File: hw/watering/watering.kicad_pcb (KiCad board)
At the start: 2 copper layers, 262 x 50 mm, 103 parts, among them J2 USB_C_Receptacle, J3 Conn_01x02_Pin, J4 Conn_01x02_Pin, J6 Conn_01x02_Pin, Q1 2N7002, SW2 KMS221GLFS, SW3 KMS221GLFS, U1 ESP32-C6, U10 MCP6002-xSN, U11 STI3508, U2 DRV8220DSG, U3 W25Q128JVS, U4 STI3508, U5 STI3508, U6 STI3508, U7 NCP163AFCT330T2G, U8 MCP6002-xSN, U9 MCP6002-xSN, Y1 40MHz, Y2 32768Hz

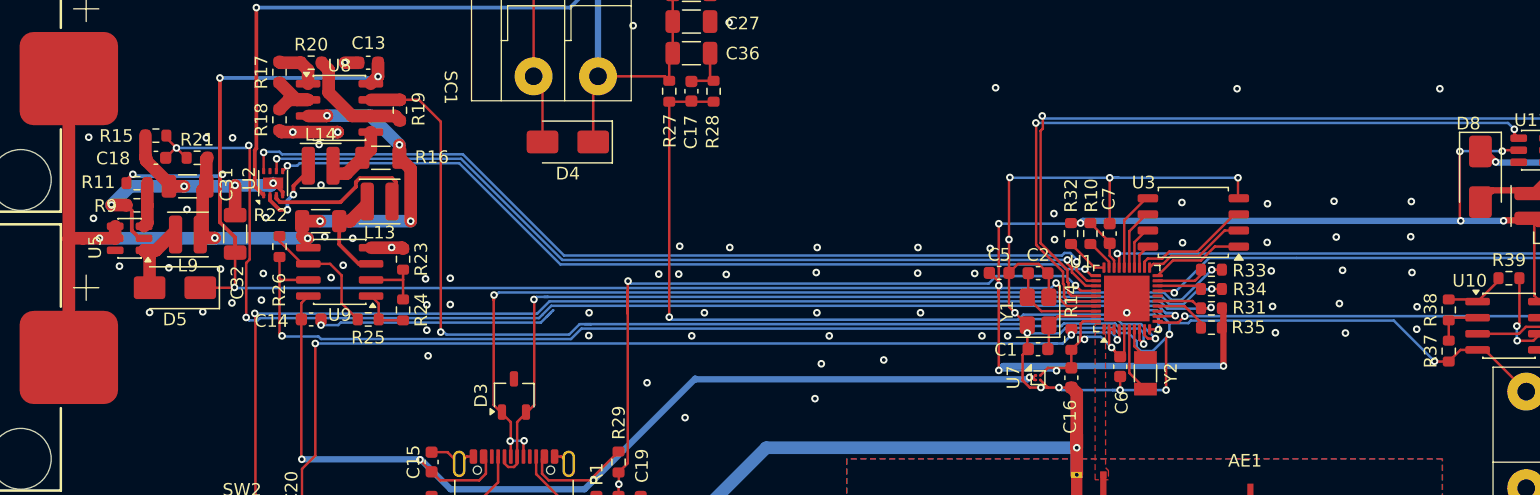
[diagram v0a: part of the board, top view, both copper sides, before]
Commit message: - improved voltage boost on battery power - some issues with rtc clock - some issues with pwm that result in brownout
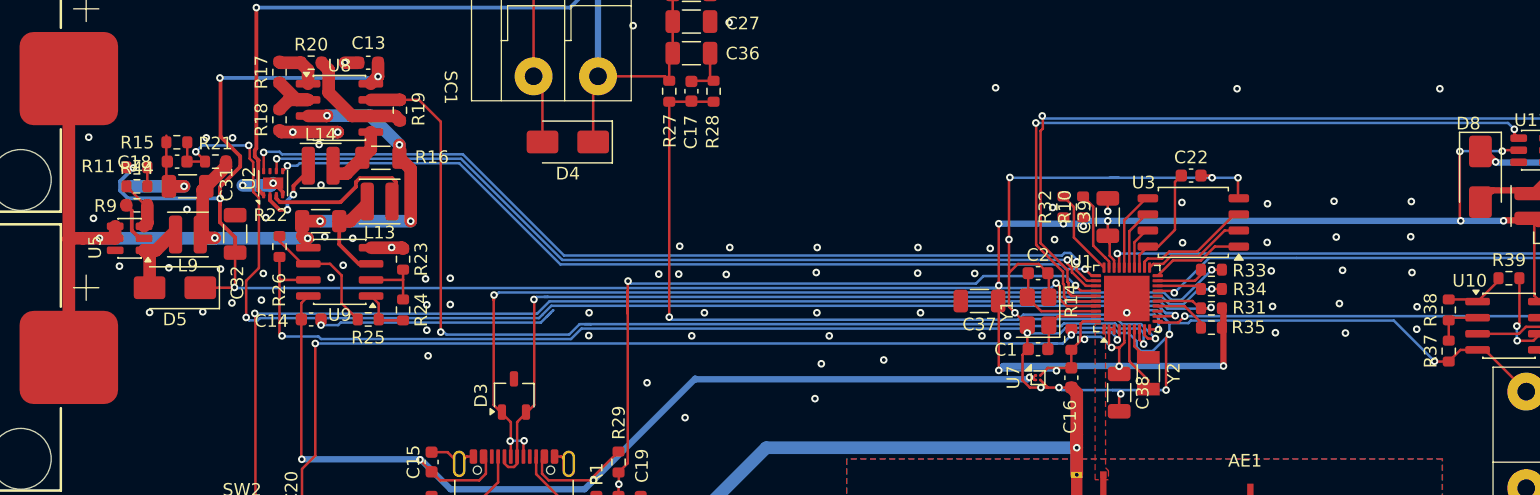
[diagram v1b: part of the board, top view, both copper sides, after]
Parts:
- removed C5, C6, C7: 100n, Capacitor_SMD:C_0603_1608Metric
- added C22: 1u, Capacitor_SMD:C_0603_1608Metric, F.Cu at (193.2, 120.7)
- added C37: 22u, Capacitor_SMD:C_1206_3216Metric, F.Cu at (176.5, 130.6)
- added C38: 22u, Capacitor_SMD:C_1206_3216Metric, F.Cu at (187.5, 137.8)
- added C39: 22u, Capacitor_SMD:C_1206_3216Metric, F.Cu at (186.6, 123.9)
- added R44: 15k, Resistor_SMD:R_0603_1608Metric, F.Cu at (110.0, 121.5)
- R11: value 47k -> 30k
- moved R32 2.18 mm to (183.1, 123.1), turned to 90 degrees
- moved R10 2.18 mm to (184.7, 123.1), turned to 90 degrees
- moved R15 1.73 mm to (113.2, 118.0)
- moved C18 1.70 mm to (113.2, 119.5)
- moved R21 1.48 mm to (116.2, 119.5)
- moved R11 1.25 mm to (110.0, 120.0)
- moved Y2 0.23 mm to (189.8, 136.2)
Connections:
- R11 pad 1: /solar/0V6 -> Net-(R11-Pad1)
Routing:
- net /GND: track 329.4 -> 317.0 mm
- net Net-(U1-VDD_SPI/GPIO27): track 1.93 -> 9.11 mm
- net /controller/SDA: track 2.51 -> 6.46 mm
- net /controller/SCL: track 3.37 -> 6.94 mm
- net /+3V3: track 299.3 -> 301.7 mm, vias 24 -> 27
- net Net-(R11-Pad1): track 0.00 -> 1.50 mm
- net /solar/0V6: track 3.51 -> 4.03 mm

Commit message: - fixed formatting - proper pwm output for conductivity output
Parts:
- removed R29: 47k, Resistor_SMD:R_0603_1608Metric
- added R45: 10k, Resistor_SMD:R_0603_1608Metric, F.Cu at (148.0, 143.2)
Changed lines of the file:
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@@
 		)
 	)
+	(footprint "Resistor_SMD:R_0603_1608Metric"
+		(layer "F.Cu")
+		(at 148 143.25 -90)
+		(descr "Resistor SMD 0603 (1608 Metric), square (rectangular) end terminal, IPC-7351 nominal, (Body size source: IPC-SM-782 page 72, https://www.pcb-3d.com/wordpress/wp-content/uploads/ipc-sm-782a_amendment_1_and_2.pdf)")
+		(tags "resistor")
+		(property "Reference" "R45"
+			(at -2.85 -0.025 90)
+			(layer "F.SilkS")
+			(effects
+				(font
+					(size 1 1)
+					(thickness 0.15)
+				)
+			)
+		)
+		(property "Value" "10k"
+			(at -0.075 -0.025 90)
+			(layer "F.Fab")
+			(effects
+				(font
+					(size 1 1)
+					(thickness 0.15)
+				)
+			)
+		)
+		(property "Datasheet" "https://jlc-prod-smt.oss-eu-central-1.aliyuncs.com/smtDataManualFile/8579706381316128768-C25804.pdf?response-content-disposition=attachment%3B%20filename%3DC25804.pdf%3B%20filename%2A%3DUTF-8%27%27C25804.pdf&x-oss-date=20260604T182440Z&x-oss-expires=1800&x-oss-security-token=CAISgAN1q6Ft5B2yfSjIr5nhDvTiu55L8aayRHLFsEERZtthpKj%2B0Dz2IHhMdHJsAOodtv0%2FmmhT6PkclqRLcbhpcmfjV%2BZHzLB8qeRniENA4J7b16cNrbH4M4H6aXeirtuwDsz9SNTCALjPD3nPii50x5bjaDymRCbLGJaViJlhHLN1Ow6jdmhpCctxLAlvo9NgFxm3D%2Fu2NQPwiWf9FVdhvhEG6Vly8qOi2MaRmFy8yFTx0b0SvJ%2BjYMrmPctoN9JnSdC5mfdzau3a1TJ84gRD0a5wkaVA1zbDs5bfISEIuUzebreLqY03dV4mOvdqIcMe8qigz88fk%2FfIioH6xyxKOexoSCnFTOiiupCcQLPyao9jLu6iayqViY7QaIOTqQohZmkAMwVOasAsI3Ngh4zF97Qt0cVNkXO9gWfLI8DtuMleWhri1Udu3tHD0eS19jklBdzSlusJRAJJUVBflCeKEaRNSAd3WGhEfM2%2BBt4QT30w5N2u00S8OSMIOONBvqKWD5sagAGpldF62iBeHzrNV%2BHnUyjaA64BCjacRbVbSjmxSgiuNX1d%2FbCnqQV25prdqNhtDbAKCoRnNQDFNxmhLIIUUcffM9eG3oRc44RNhyi7hADN6z1ILjt6TEoRuXkDAYH1u8iyrE2YQDMkq7F3Cke8dxQ44PYZqWefci6GHDzQ1pzPpiAA&x-oss-signature-version=OSS4-HMAC-SHA256&x-oss-credential=STS.NZTENVVAjFdYFTtTADjTMKmU2%2F20260604%2Feu-central-1%2Foss%2Faliyun_v4_request&x-oss-signature=78c2b620008555fdaf271c3d0b7682edd0aca7d23428d31f63338848e1713cab"
+			(at 0 0 90)
+			(layer "F.Fab")
+			(hide yes)
+			(effects
+				(font
+					(size 1.27 1.27)
+				)
+			)
+		)
+		(property "Description" "C25804"
+			(at 0 0 90)
+			(layer "F.Fab")
+			(hide yes)
+			(effects
+				(font
+					(size 1.27 1.27)
+				)
+			)
+		)
+		(property "KiLib_Generator" "SMD_2terminal_chip_molded"
+			(at 0 0 90)
+			(layer "F.SilkS")
+			(hide yes)
+			(effects
+				(font
+					(size 1 1)
+					(thickness 0.15)
+				)
+			)
+		)
+		(property ki_fp_filters "R_*")
+		(sheetname "/")
+		(sheetfile "watering.kicad_sch")
+		(units
+			(unit
+				(name "A")
+				(pins "1" "2")
+			)
+		)
+		(attr smd)
+		(duplicate_pad_numbers_are_jumpers no)
+		(fp_line
+			(start -0.237258 0.5225)
+			(end 0.237258 0.5225)
+			(stroke
+				(width 0.12)
+				(type solid)
+			)
+			(layer "F.SilkS")
+		)
+		(fp_line
+			(start -0.237258 -0.5225)
+			(end 0.237258 -0.5225)
+			(stroke
+				(width 0.12)
+				(type solid)
+			)
+			(layer "F.SilkS")
+		)
+		(fp_rect
+			(start -1.48 -0.73)
+			(end 1.48 0.73)
+			(stroke
+				(width 0.05)
+				(type solid)
+			)
+			(fill no)
+			(layer "F.CrtYd")
+		)
+		(fp_rect
+			(start -0.8 -0.4125)
+			(end 0.8 0.4125)
+			(stroke
+				(width 0.1)
+				(type solid)
+			)
+			(fill no)
+			(layer "F.Fab")
+		)
+		(fp_text user "${REFERENCE}"
+			(at 0 0 90)
+			(layer "F.Fab")
+			(effects
+				(font
+					(size 0.4 0.4)
+					(thickness 0.06)
+				)
+			)
+		)
+		(pad "1" smd roundrect
+			(at -0.825 0 270)
+			(size 0.8 0.95)
+			(layers "F.Cu" "F.Mask" "F.Paste")
+			(roundrect_rratio 0.25)
+			(net "/+5V")
+			(pintype "passive")
+		)
+		(pad "2" smd roundrect
+			(at 0.825 0 270)
+			(size 0.8 0.95)
+			(layers "F.Cu" "F.Mask" "F.Paste")
+			(roundrect_rratio 0.25)
+			(net "/V_usb_avail")
+			(pintype "passive")
+		)
+		(embedded_fonts no)
+		(model "${KICAD10_3DMODEL_DIR}/Resistor_SMD.3dshapes/R_0603_1608Metric.step"
+			(offset
+				(xyz 0 0 0)
+			)
+			(scale
+				(xyz 1 1 1)
+			)
+			(rotate
+				(xyz 0 0 0)
+			)
+		)
+	)
 	(footprint "Capacitor_SMD:C_1206_3216Metric"
 		(layer "F.Cu")
@@
 		(tags "capacitor")
 		(property "Reference" "C38"
-			(at 0 -1.85 90)
+			(at 3.825 -0.175 90)
 			(layer "F.SilkS")
 			(effects
@@
 		)
 		(property "Value" "22u"
-			(at 0 1.85 90)
+			(at 0.05 0 90)
 			(layer "F.Fab")
 			(effects
@@
 			(layer "F.Fab")
 		)
-		(fp_text user "${REFERENCE}"
-			(at 0 0 90)
-			(layer "F.Fab")
-			(effects
-				(font
-					(size 0.8 0.8)
-					(thickness 0.12)
-				)
-			)
-		)
 		(pad "1" smd roundrect
 			(at -1.475 0 270)
@@
 		)
 	)
-	(footprint "Resistor_SMD:R_0603_1608Metric"
-		(layer "F.Cu")
-		(at 148 143.25 90)
-		(descr "Resistor SMD 0603 (1608 Metric), square (rectangular) end terminal, IPC-7351 nominal, (Body size source: IPC-SM-782 page 72, https://www.pcb-3d.com/wordpress/wp-content/uploads/ipc-sm-782a_amendment_1_and_2.pdf)")
-		(tags "resistor")
-		(property "Reference" "R29"
-			(at 3.1 0.025 90)
-			(layer "F.SilkS")
-			(effects
-				(font
-					(size 1 1)
-					(thickness 0.15)
-				)
-			)
-		)
-		(property "Value" "47k"
-			(at -0.025 0.125 90)
-			(layer "F.Fab")
-			(effects
-				(font
-					(size 1 1)
-					(thickness 0.15)
-				)
-			)
-		)
-		(property "Datasheet" "https://jlc-prod-smt.oss-eu-central-1.aliyuncs.com/smtDataManualFile/8579706364622934016-C25819.pdf?response-content-disposition=attachment%3B%20filename%3DC25819.pdf%3B%20filename%2A%3DUTF-8%27%27C25819.pdf&x-oss-date=20260607T210642Z&x-oss-expires=1800&x-oss-security-token=CAISgAN1q6Ft5B2yfSjIr5ryH8PCprRbhIysal7ylzcBXuxKqZznuzz2IHhMdHJsAOodtv0%2FmmhT6PkclqRLcbhpcmfjV%2BZHzLB8qbxek0BD4J7b16cNrbH4M4H6aXeirtuwDsz9SNTCALjPD3nPii50x5bjaDymRCbLGJaViJlhHLN1Ow6jdmhpCctxLAlvo9NgFxm3D%2Fu2NQPwiWf9FVdhvhEG6Vly8qOi2MaRmFy8yFTx0b0SvJ%2BjYMrmPctoN9JnSdC5mfdzau3a1TJ84gRD0a5wkaVA1zbDs5bfISEIuUzebreLqY03dV4mOvdqIcMe8qigz88fk%2FfIioH6xyxKOexoSCnFTOiiupCcQLPyao9jLu6iayqViY7QaIOTqQohZmkAMwVOasAsI3Ngh4zF97Qt0cVNkXO9gWfLI8DtuMleWkpjUPw8wnSgc5lCkRRYwGs1287ugXlSQzo890KPDAEovaKCnZ2ZSfh7Y4sNknI6i%2Bfc2Se2MIkIuzN54aKWD5sagAFXqr37yeC6i73JtnWyrAPWlFlD7%2BO4v6D0kklJkfR4ZNWYY%2FJmHaMvh5XgKe69Y2VVwh3FQXeQc9N3YnYUCwlUFj7ysfoRU0zIPvuKAhEOT3qEObty6yli3txhJK%2BkEcQ4NQs%2FlNRRqPdiq%2BB4j8AoteNyHTVnRr3qFmKb96GmHCAA&x-oss-signature-version=OSS4-HMAC-SHA256&x-oss-credential=STS.NYGTyvKkz3NGhxCs7TRcfFYLY%2F20260607%2Feu-central-1%2Foss%2Faliyun_v4_request&x-oss-signature=d302d6996d62a00132e559a883be9b5fca7841b1eb7e44c91ba09bae985432b1"
-			(at 0 0 90)
-			(layer "F.Fab")
-			(hide yes)
-			(effects
-				(font
-					(size 1.27 1.27)
-				)
-			)
-		)
-		(property "Description" "C25819"
-			(at 0 0 90)
-			(layer "F.Fab")
-			(hide yes)
-			(effects
-				(font
-					(size 1.27 1.27)
-				)
-			)
-		)
-		(property "KiLib_Generator" "SMD_2terminal_chip_molded"
-			(at 0 0 90)
-			(layer "F.SilkS")
-			(hide yes)
-			(effects
-				(font
-					(size 1 1)
-					(thickness 0.15)
-				)
-			)
-		)
-		(property ki_fp_filters "R_*")
-		(sheetname "/")
-		(sheetfile "watering.kicad_sch")
-		(units
-			(unit
-				(name "A")
-				(pins "1" "2")
-			)
-		)
-		(attr smd)
-		(duplicate_pad_numbers_are_jumpers no)
-		(fp_line
-			(start -0.237258 -0.5225)
-			(end 0.237258 -0.5225)
-			(stroke
-				(width 0.12)
-				(type solid)
-			)
-			(layer "F.SilkS")
-		)
-		(fp_line
-			(start -0.237258 0.5225)
-			(end 0.237258 0.5225)
-			(stroke
-				(width 0.12)
-				(type solid)
-			)
-			(layer "F.SilkS")
-		)
-		(fp_rect
-			(start -1.48 -0.73)
-			(end 1.48 0.73)
-			(stroke
-				(width 0.05)
-				(type solid)
-			)
-			(fill no)
-			(layer "F.CrtYd")
-		)
-		(fp_rect
-			(start -0.8 -0.4125)
-			(end 0.8 0.4125)
-			(stroke
-				(width 0.1)
-				(type solid)
-			)
-			(fill no)
-			(layer "F.Fab")
-		)
-		(pad "1" smd roundrect
-			(at -0.825 0 90)
-			(size 0.8 0.95)
-			(layers "F.Cu" "F.Mask" "F.Paste")
-			(roundrect_rratio 0.25)
-			(net "/V_usb_avail")
-			(pintype "passive")
-		)
-		(pad "2" smd roundrect
-			(at 0.825 0 90)
-			(size 0.8 0.95)
-			(layers "F.Cu" "F.Mask" "F.Paste")
-			(roundrect_rratio 0.25)
-			(net "/+5V")
-			(pintype "passive")
-		)
-		(embedded_fonts no)
-		(model "${KICAD10_3DMODEL_DIR}/Resistor_SMD.3dshapes/R_0603_1608Metric.step"
-			(offset
-				(xyz 0 0 0)
-			)
-			(scale
-				(xyz 1 1 1)
-			)
-			(rotate
-				(xyz 0 0 0)
-			)
-		)
-	)
 	(footprint "DORABO:DB142R-5.08-2P-GN"
 		(layer "F.Cu")
@@
 	)
 	(segment
+		(start 183.925 125.5375)
+		(end 183.925 123.125)
+		(width 0.2)
+		(layer "F.Cu")
+		(net "/controller/SCL")
+	)
+	(segment
+		(start 186.3 127.9125)
+		(end 183.925 125.5375)
+		(width 0.2)
+		(layer "F.Cu")
+		(net "/controller/SCL")
+	)
+	(segment
+		(start 183.925 123.125)
+		(end 183.1 122.3)
+		(width 0.2)
+		(layer "F.Cu")
+		(net "/controller/SCL")
+	)
+	(segment
 		(start 118.9 119.315686)
 		(end 119.175 119.590685)
@@
 	)
 	(segment
-		(start 183.925 125.5375)
-		(end 183.925 123.125)
-		(width 0.2)
-		(layer "F.Cu")
-		(net "/controller/SCL")
-	)
-	(segment
-		(start 186.3 127.9125)
-		(end 183.925 125.5375)
-		(width 0.2)
-		(layer "F.Cu")
-		(net "/controller/SCL")
-	)
-	(segment
-		(start 183.925 123.125)
-		(end 183.1 122.3)
-		(width 0.2)
-		(layer "F.Cu")
-		(net "/controller/SCL")
-	)
-	(segment

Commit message: hw mods
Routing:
- net /+5V: track 113.7 -> 110.2 mm, vias 4 -> 5
- net /controller/v2: track 65.3 -> 63.1 mm
- net /GND: track 317.0 -> 315.1 mm
- net /+3V3: track 301.7 -> 302.2 mm
- net /controller/reset: track 82.4 -> 83.0 mm

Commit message: - sw   - charging batteries with solar somewhat works. mppt tracking is not possible because i messed up the current measurement   - implemented pid controller for current control. not operative, since current meas isn't working. maybe a voltage correlation is possibe? - hw   - current measurement is bad. output voltage of usb current is not high enough since input voltages are higher   - usb voltage wasn't connected correctly for charging   - solving by making battery voltage the main voltage bus on pcb and have all voltage users capped by switches to prevent battery drainage
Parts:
- removed U2: DRV8220DSG, Package_SON:WSON-8-1EP_2x2mm_P0.5mm_EP0.9x1.6mm
- added C3: 15p, Capacitor_SMD:C_0603_1608Metric, F.Cu at (161.9, 91.6)
- added C4: 15p, Capacitor_SMD:C_0603_1608Metric, F.Cu at (161.9, 94.1)
- added C40: 22u, Capacitor_SMD:C_1206_3216Metric, F.Cu at (162.7, 76.6)
- added C41: 22u, Capacitor_SMD:C_1206_3216Metric, F.Cu at (162.7, 80.0)
- added C42: 22u, Capacitor_SMD:C_1206_3216Metric, F.Cu at (162.7, 83.3)
- added C43: 22u, Capacitor_SMD:C_1206_3216Metric, F.Cu at (162.7, 86.7)
- BT1, BT2: moved to B.Cu
- moved C20 144.1 mm to (264.2, 124.1), turned to 0 degrees
- moved SW2 142.2 mm to (258.7, 125.1)
- moved U8 140.7 mm to (266.6, 109.5)
- moved R18 139.2 mm to (260.4, 112.4), turned to 0 degrees
- moved R17 139.2 mm to (260.4, 109.9), turned to 0 degrees
- moved L14 138.4 mm to (262.0, 136.2)
- moved C15 137.7 mm to (270.2, 128.6), turned to 0 degrees
- moved R20 136.7 mm to (260.4, 117.4)
- moved R16 136.0 mm to (265.2, 114.4)
- moved SW3 133.9 mm to (258.7, 129.6), turned to 0 degrees
- moved C13 132.2 mm to (260.4, 107.4), turned to 0 degrees
- moved REF** 130.0 mm to (146.3, 104.5)
- moved R19 129.6 mm to (260.4, 114.9), turned to 0 degrees
- moved L13 129.0 mm to (257.4, 136.2), turned to 0 degrees
- moved R22 123.2 mm to (247.5, 131.0)
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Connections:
- net /solar/0V6 renamed /solar/bat/0V6
- BT1 pad 1: /solar/V_bat -> /V_bat
- BT2 pad 1: /solar/V_bat -> /V_bat
- C13 pad 1: /+3V3 -> /solar/+Vsolar
- C21 pad 1: /+3V3 -> /V_bat
- C31 pad 1: /solar/V_bat -> /V_bat
- C34 pad 1: /+3V3 -> /V_bat
- L13 pad 2: /solar/current_meas1/i_out -> /solar/current_meas/i_out
- L14 pad 2: /solar/current_meas/i_in -> /solar/current_meas1/i_out
- L8 pad 1: /+3V3 -> /V_bat
- L9 pad 1: /solar/V_bat -> /V_bat
- R16 pad 1: /solar/current_meas/i_in -> /solar/+Vsolar
- R16 pad 2: /solar/V_bat -> /solar/current_meas/i_out
- R21 pad 2: /solar/V_bat -> /V_bat
- R22 pad 1: /solar/V_bat -> /+5V
- U10 pad 8: /+3V3 -> /V_bat
- U11 pad 5: /+3V3 -> /V_bat
- U5 pad 4: /solar/V_bat -> /V_bat
- U5 pad 5: /solar/V_bat -> /V_bat
- U8 pad 3: /solar/V_bat -> /solar/current_meas/i_out
- U8 pad 5: /solar/current_meas/i_in -> /solar/+Vsolar
- U8 pad 8: /+3V3 -> /solar/+Vsolar
- U9 pad 5: /solar/V_bat -> /+5V
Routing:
- net /GND: track 315.1 -> 0.00 mm, vias 127 -> 0
- net /+3V3: track 302.2 -> 0.00 mm, vias 27 -> 0
- net /+5V: track 110.2 -> 0.00 mm, vias 5 -> 0
- net /controller/V_bat_meas: track 98.7 -> 0.00 mm, vias 4 -> 0
- net /controller/boot: track 98.3 -> 0.00 mm, vias 2 -> 0
- net /controller/reset: track 83.0 -> 0.00 mm, vias 3 -> 0
- net /controller/i_meas_solar: track 82.4 -> 0.00 mm, vias 2 -> 0
- net /controller/i_usb_meas: track 79.7 -> 0.00 mm, vias 2 -> 0
- net /solar/V_bat: track 78.0 -> 0.00 mm, vias 7 -> 0
- net /solar/+Vsolar: track 75.3 -> 0.00 mm, vias 1 -> 0
- net /controller/USBDP: track 74.1 -> 0.00 mm, vias 4 -> 0
- net /controller/pwm-enable: track 72.1 -> 0.00 mm, vias 2 -> 0
- net /controller/USBDM: track 70.2 -> 0.00 mm, vias 2 -> 0
- net /controller/solar-pwm: track 70.1 -> 0.00 mm, vias 2 -> 0
- net /controller/usb-pwm: track 68.1 -> 0.00 mm, vias 2 -> 0
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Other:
- board size 262 x 50 mm -> 96.8 x 50.1 mm
